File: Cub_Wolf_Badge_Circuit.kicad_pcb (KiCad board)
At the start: 2 copper layers, 49.5 x 68.3 mm, 13 parts, among them Q1 2N3904, Q2 2N3904, SW1 SW_SPDT

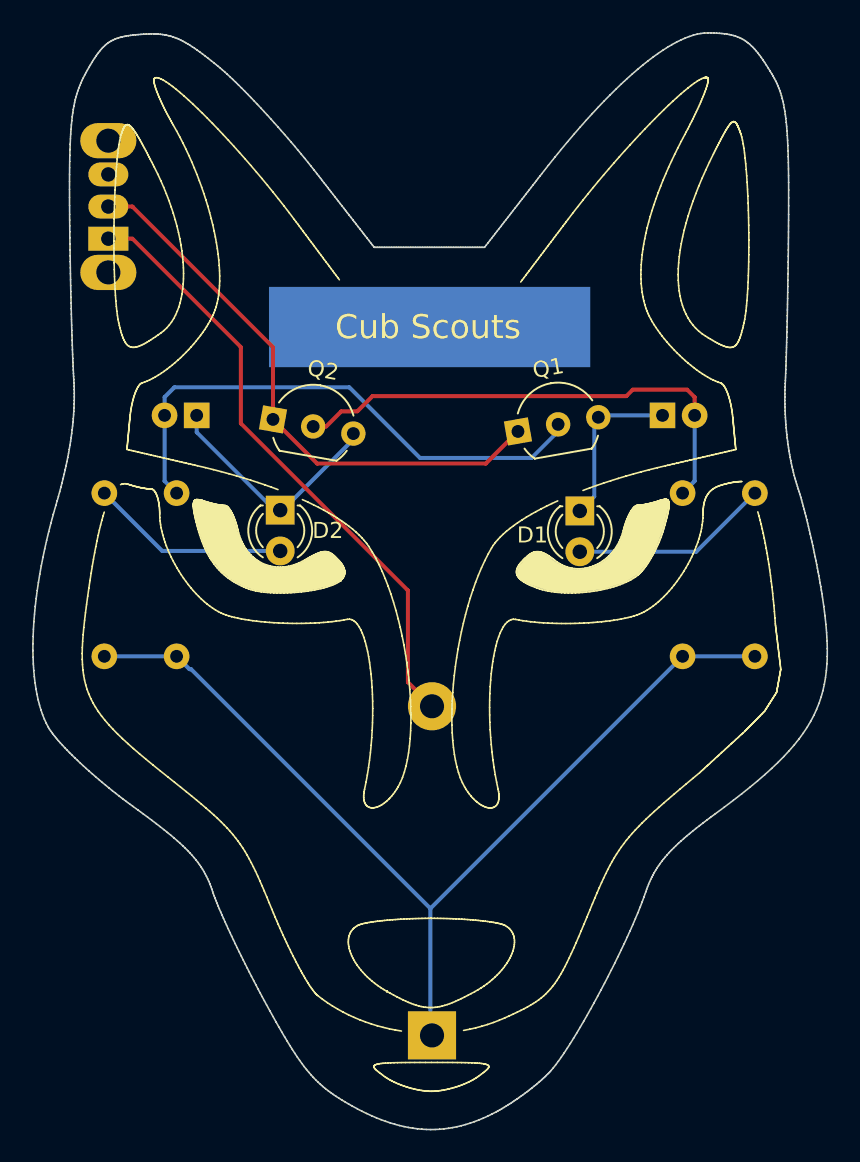
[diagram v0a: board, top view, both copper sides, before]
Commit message: Updated trace placement on switch, updated resistor values.
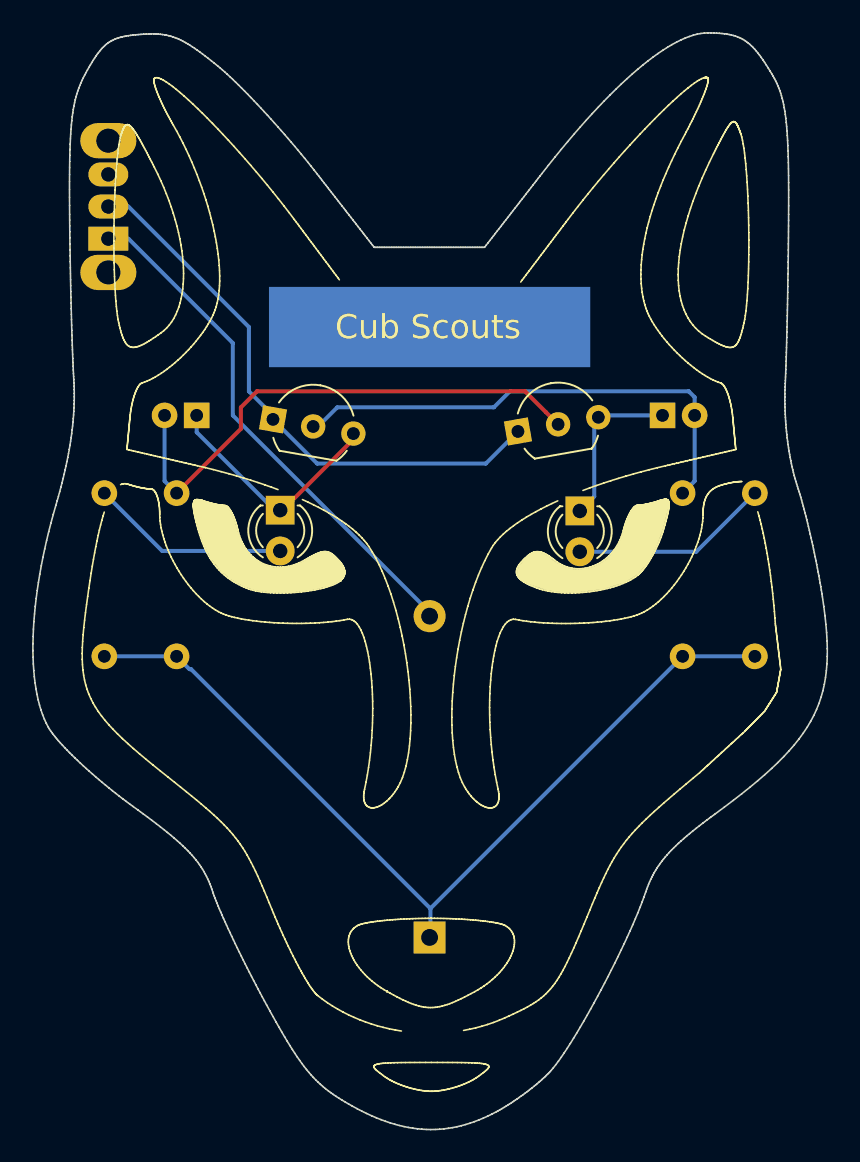
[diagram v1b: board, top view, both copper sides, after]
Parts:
- BT1: footprint Battery_Holders:Keystone_106_1x20mm-CoinCell -> MyParts:1x20mm-CoinCell
- moved BT1 18.1 mm to (126.2, 70.5)
- renumbered D1 to LED1, D2 to LED2, Q1 to Transistor1, Q2 to Transistor2
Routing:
- net Net-(BT1-Pad1): track 62.0 -> 55.3 mm
- net Net-(BT1-Pad2): track 38.3 -> 32.3 mm
- net Net-(C2-Pad2): track 34.0 -> 33.2 mm
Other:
- rule pad_to_mask_clearance: 0.2 -> 0.1
